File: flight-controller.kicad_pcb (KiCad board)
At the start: 4 copper layers, 36 x 36 mm, 107 parts, among them J1 USB_C_Receptacle_USB2.0, Q1 AO3400A, SW1 SW_Push, U1 AT32F435RGT7, U2 BMI270, U3 BMP280, U4 W25N01GVZEIG, U5 AT7456E, U6 TPS54302, U7 TPS54302, U8 TLV75733PDBV, U9 USBLC6-2P6, Y1 27MHz

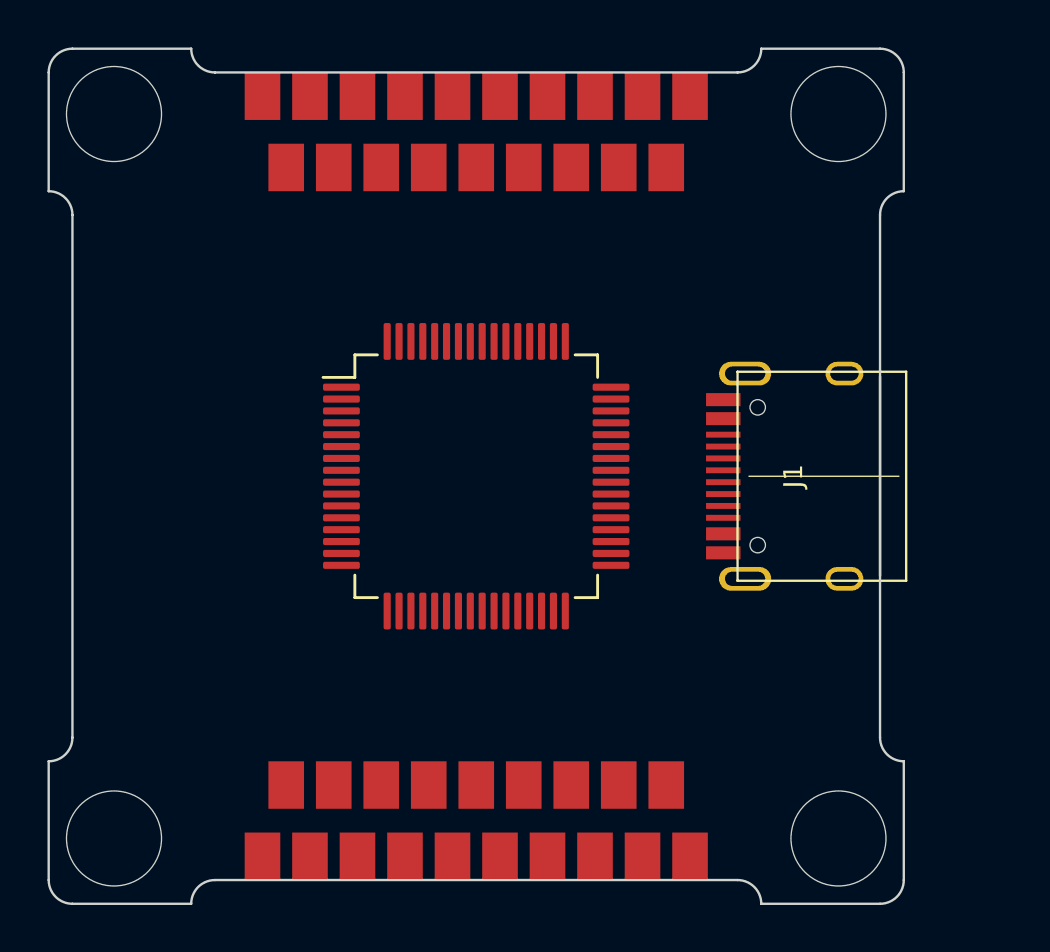
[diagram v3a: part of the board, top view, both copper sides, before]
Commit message: Add JST connectors
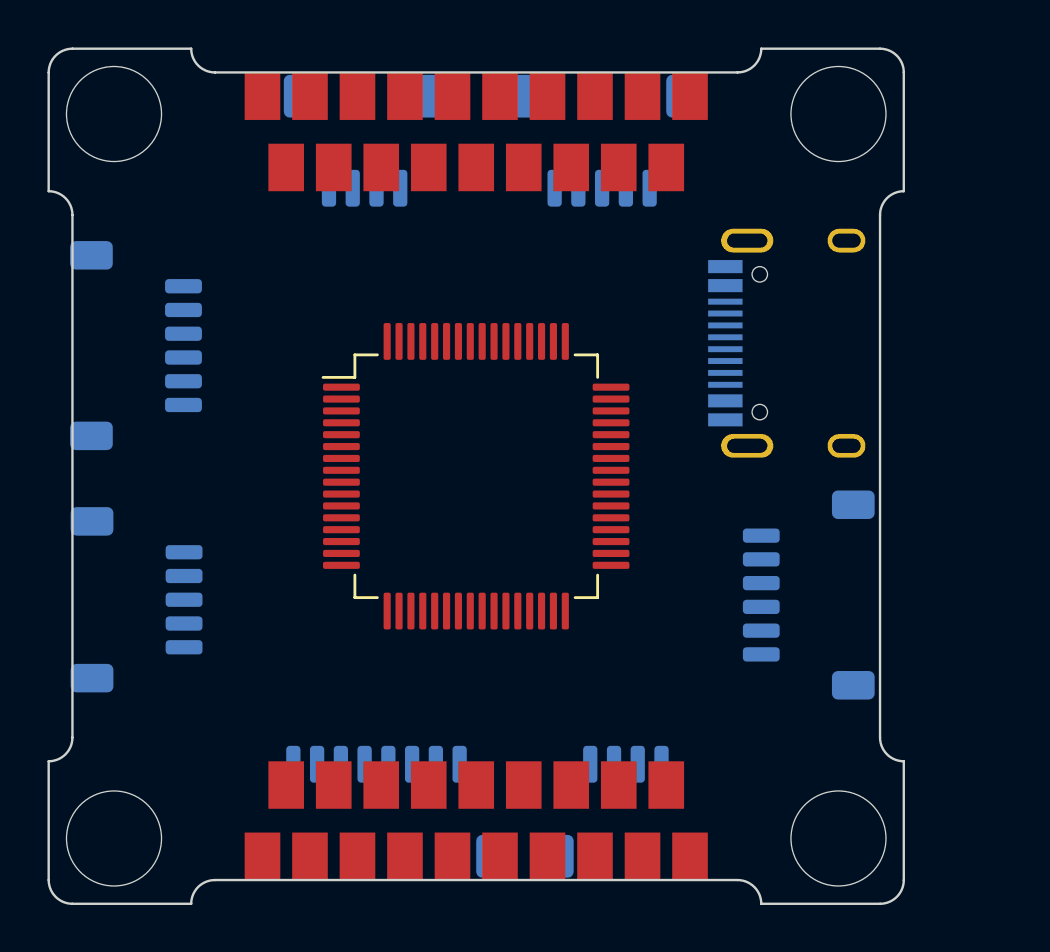
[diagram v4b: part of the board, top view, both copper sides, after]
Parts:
- added J2: ESC, Connector_JST:JST_SH_SM08B-SRSS-TB_1x08-1MP_P1.00mm_Horizontal, B.Cu at (113.8, 117.1)
- added J3: RX, Connector_JST:JST_SH_SM04B-SRSS-TB_1x04-1MP_P1.00mm_Horizontal, B.Cu at (113.3, 88.9)
- added J4: GPS, Connector_JST:JST_SH_SM06B-SRSS-TB_1x06-1MP_P1.00mm_Horizontal, B.Cu at (103.7, 97.5)
- added J5: I2C, Connector_JST:JST_SH_SM04B-SRSS-TB_1x04-1MP_P1.00mm_Horizontal, B.Cu at (124.3, 117.1)
- added J6: Camera, Connector_JST:JST_SH_SM05B-SRSS-TB_1x05-1MP_P1.00mm_Horizontal, B.Cu at (103.7, 108.2)
- added J7: VTX, Connector_JST:JST_SH_SM05B-SRSS-TB_1x05-1MP_P1.00mm_Horizontal, B.Cu at (123.3, 88.9)
- added J8: DVTX, Connector_JST:JST_SH_SM06B-SRSS-TB_1x06-1MP_P1.00mm_Horizontal, B.Cu at (132.0, 108.0)
- J1: moved to B.Cu
- moved J1 5.60 mm to (133.6, 97.4), turned to -90 degrees
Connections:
- U1 pad 10: ISENSE -> UART8_TX
- U1 pad 11: VSENSE -> UART8_RX
- U1 pad 14: UART4_TX -> ISENSE
- U1 pad 15: UART4_RX -> VSENSE
- U1 pad 31: unconnected-(U1-PH3-Pad31) -> UART4_TX
- U1 pad 41: unconnected-(U1-PA8-Pad41) -> TMR1_CH1
- U1 pad 47: unconnected-(U1-PH2-Pad47) -> UART4_RX
- U1 pad 5: unconnected-(U1-PH0-Pad5) -> I2C1_SDA
- U1 pad 50: unconnected-(U1-PA15-Pad50) -> SPI3_CS
- U1 pad 53: unconnected-(U1-PC12-Pad53) -> UART5_TX
- U1 pad 54: SPI3_CS -> UART5_RX
- U1 pad 6: unconnected-(U1-PH1-Pad6) -> I2C1_SCL
- U1 pad 8: I2C3_SCL -> UART7_TX
- U1 pad 9: I2C3_SDA -> UART7_RX

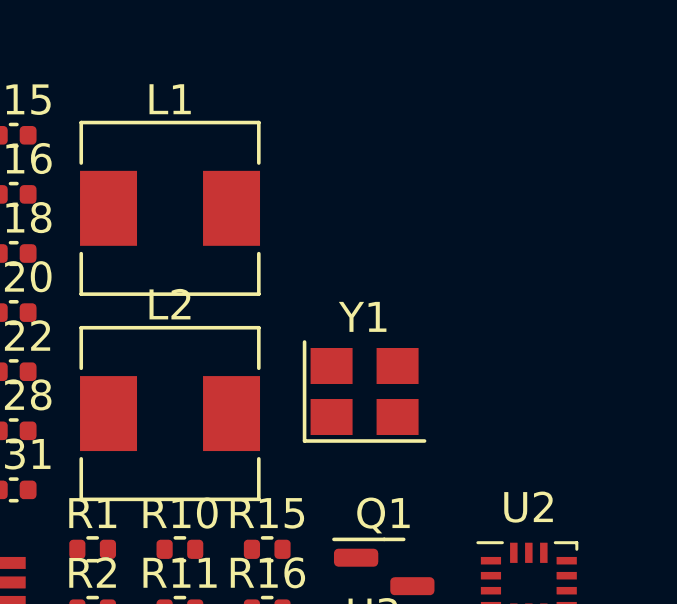
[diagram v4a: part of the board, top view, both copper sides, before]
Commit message: Add AT32 HSE crystal and choose LED resistors
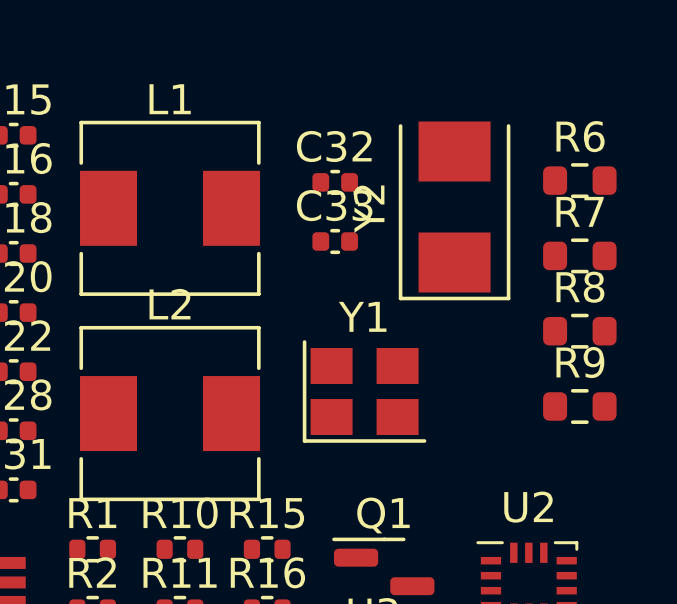
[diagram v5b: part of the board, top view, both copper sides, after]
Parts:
- added C32: 22pf, Capacitor_SMD:C_0402_1005Metric, F.Cu at (167.0, 89.0)
- added C33: 22pf, Capacitor_SMD:C_0402_1005Metric, F.Cu at (167.0, 91.0)
- added R6: 390, Resistor_SMD:R_0603_1608Metric, F.Cu at (175.2, 89.0)
- added R7: 100, Resistor_SMD:R_0603_1608Metric, F.Cu at (175.2, 91.5)
- added R8: 180, Resistor_SMD:R_0603_1608Metric, F.Cu at (175.2, 94.0)
- added R9: 180, Resistor_SMD:R_0603_1608Metric, F.Cu at (175.2, 96.5)
- added Y2: 8MHz, Crystal:Crystal_SMD_5032-2Pin_5.0x3.2mm, F.Cu at (171.0, 89.8)
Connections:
- J4 pad 5: I2C3_SDA -> I2C2_SDA
- J4 pad 6: I2C3_SCL -> I2C2_SCL
- J5 pad 3: I2C3_SDA -> I2C2_SDA
- J5 pad 4: I2C3_SCL -> I2C2_SCL
- J6 pad 4: USART7_RX -> UART7_RX
- J6 pad 5: USART7_TX -> UART7_TX
- J7 pad 4: UART5_RX -> USART3_TX
- J7 pad 5: UART5_TX -> USART3_RX
- J8 pad 6: UART4_RX -> UART5_RX
- U1 pad 31: UART4_TX -> I2C2_SDA
- U1 pad 47: UART4_RX -> I2C2_SCL
- U1 pad 5: I2C1_SDA -> HEXT_IN
- U1 pad 6: I2C1_SCL -> HEXT_OUT

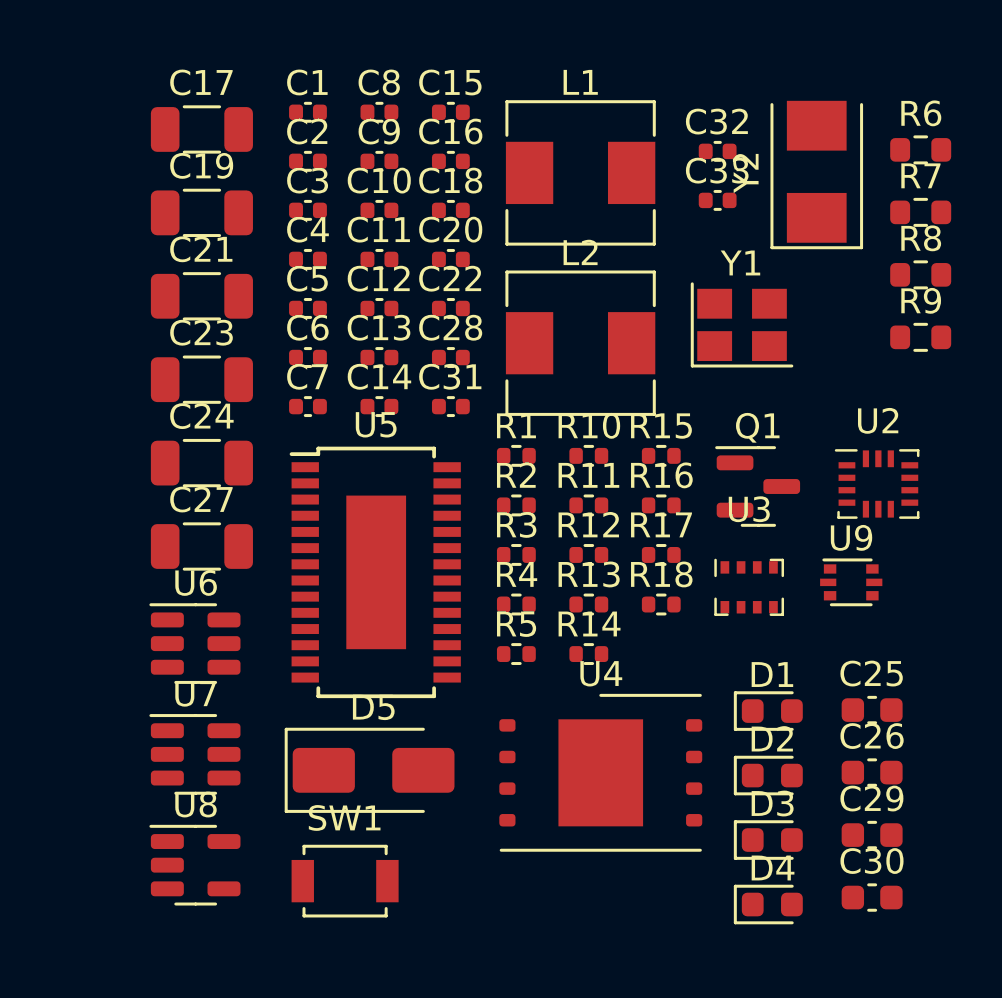
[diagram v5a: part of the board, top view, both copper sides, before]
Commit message: Change LED resistors to reduce current, tidy up schematic sheet, changes to AT32 pinout
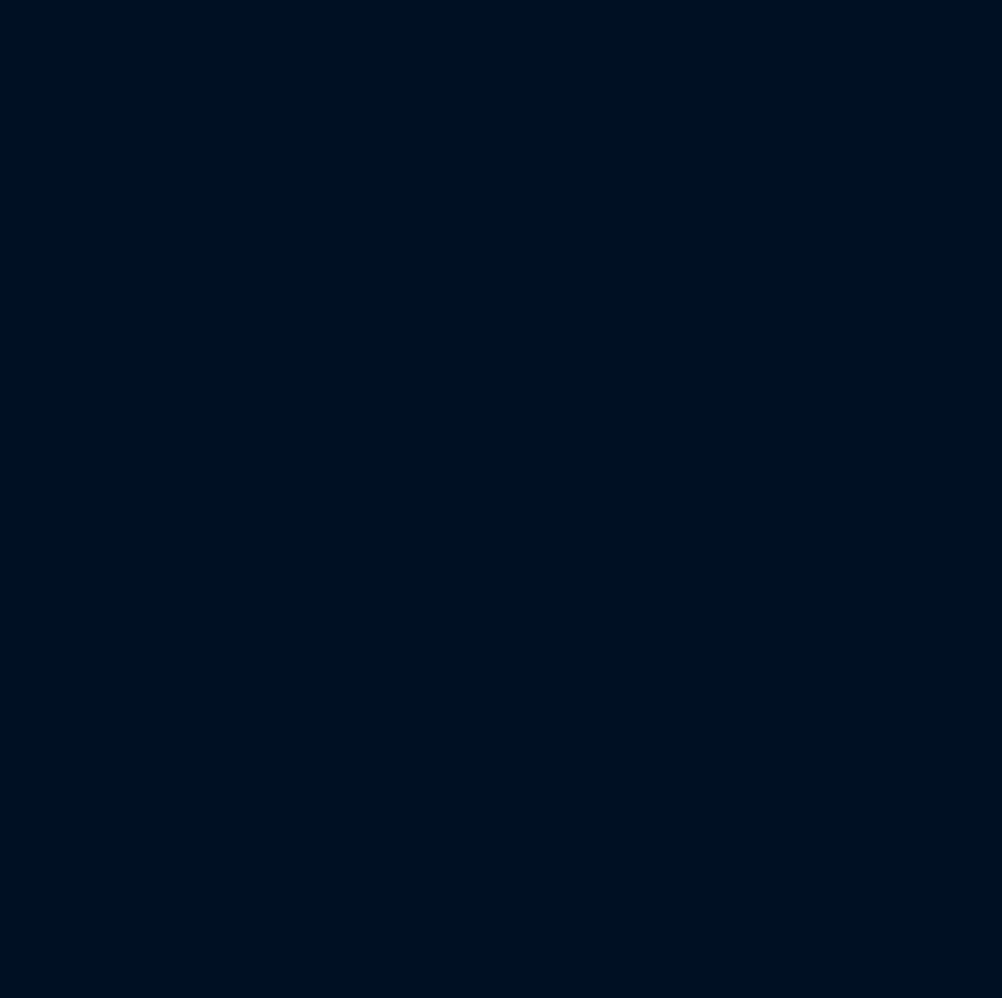
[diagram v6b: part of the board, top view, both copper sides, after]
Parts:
- removed C1, C10, C11, C12, C13, C14, C15, C18, C2, C20, C28, C3, C31, C4, C5, C6, C7, C8, C9: 100n, Capacitor_SMD:C_0402_1005Metric
- removed C16, C22: 68p, Capacitor_SMD:C_0402_1005Metric
- removed C17, C23, C24, C27: 22u, Capacitor_SMD:C_1206_3216Metric
- removed C19, C21: 10u 50V, Capacitor_SMD:C_1206_3216Metric
- removed C25, C26, C29, C30: 10u, Capacitor_SMD:C_0603_1608Metric
- removed C32, C33: 22pf, Capacitor_SMD:C_0402_1005Metric
- removed D1: BLUE, LED_SMD:LED_0603_1608Metric
- removed D2: GREEN, LED_SMD:LED_0603_1608Metric
- removed D3: RED, LED_SMD:LED_0603_1608Metric
- removed D4: YELLOW, LED_SMD:LED_0603_1608Metric
- removed D5: SS34, Diode_SMD:D_SMA
- removed L1, L2: 10u, Inductor_SMD:L_Sunlord_MWSA0503S
- removed Q1: AO3400A, Package_TO_SOT_SMD:SOT-23
- removed R1, R14, R18, R4, R5: 10k, Resistor_SMD:R_0402_1005Metric
- removed R10, R12, R17: 100k, Resistor_SMD:R_0402_1005Metric
- removed R11: 6.34k, Resistor_SMD:R_0402_1005Metric
- removed R13: 13.3k, Resistor_SMD:R_0402_1005Metric
- removed R15, R16: 75, Resistor_SMD:R_0402_1005Metric
- removed R2, R3: 5.1k, Resistor_SMD:R_0402_1005Metric
- removed R6: 390, Resistor_SMD:R_0603_1608Metric
- removed R7: 100, Resistor_SMD:R_0603_1608Metric
- removed R8, R9: 180, Resistor_SMD:R_0603_1608Metric
- removed SW1: SW_Push, Button_Switch_SMD:SW_SPST_B3U-1000P
- removed U2: BMI270, Package_LGA:Bosch_LGA-14_3x2.5mm_P0.5mm
- removed U3: BMP280, Package_LGA:Bosch_LGA-8_2x2.5mm_P0.65mm_ClockwisePinNumbering
- removed U4: W25N01GVZEIG, Package_SON:WSON-8-1EP_8x6mm_P1.27mm_EP3.4x4.3mm
- removed U5: AT7456E, Package_SO:TSSOP-28-1EP_4.4x9.7mm_P0.65mm
- removed U6, U7: TPS54302, Package_TO_SOT_SMD:SOT-23-6
- removed U8: TLV75733PDBV, Package_TO_SOT_SMD:SOT-23-5
- removed U9: USBLC6-2P6, Package_TO_SOT_SMD:SOT-666
- removed Y1: 27MHz, Crystal:Crystal_SMD_3225-4Pin_3.2x2.5mm
- removed Y2: 8MHz, Crystal:Crystal_SMD_5032-2Pin_5.0x3.2mm
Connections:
- J2 pad 4: UART8_RX -> UART5_RX
- J6 pad 4: UART7_RX -> UART4_RX
- J6 pad 5: UART7_TX -> UART4_TX
- J8 pad 6: UART5_RX -> UART6_RX
- U1 pad 14: ISENSE -> UART4_TX
- U1 pad 15: VSENSE -> UART4_RX
- U1 pad 2: unconnected-(U1-PC13-Pad2) -> 10V_SW
- U1 pad 24: TMR9_CH1 -> USART3_TX
- U1 pad 25: TMR9_CH2 -> USART3_RX
- U1 pad 37: TIM3_CH1 -> TMR3_CH1
- U1 pad 38: TIM3_CH2 -> TMR3_CH2
- U1 pad 39: TIM3_CH3 -> TMR3_CH3
- U1 pad 4: 10V_SW -> unconnected-(U1-PC15-Pad4)
- U1 pad 40: TIM3_CH4 -> TMR3_CH4
- U1 pad 51: USART3_TX -> TMR5_CH2
- U1 pad 52: USART3_RX -> TMR5_CH3
- U1 pad 8: UART7_TX -> VSENSE
- U1 pad 9: UART7_RX -> ISENSE
